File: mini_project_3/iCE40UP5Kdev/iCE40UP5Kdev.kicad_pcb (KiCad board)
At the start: 2 copper layers, 51 parts, among them J1 USB4105-GF-A, J2 Left, J3 Right, U1 W25Q32JV, U2 MIC5365-1-2YD5, U3 MIC5318-3-3YD5, U4 ICE40UP5K-SG48ITR, X1 IQXO-791

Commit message: Add start to layout of mini project 3
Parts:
- J1: footprint Connector_USB:USB_C_Receptacle_GCT_USB4105-xx-A_16P_TopMnt_Horizontal -> Eclectronics:USB4105-GF-A
- moved C2 110.6 mm to (154.7, 97.2), turned to 180 degrees
- moved C1 109.5 mm to (155.5, 91.5)
- moved C7 108.2 mm to (155.2, 104.7), turned to 90 degrees
- moved U4 107.4 mm to (150.3, 113.2), turned to 180 degrees
- moved R16 102.3 mm to (153.5, 107.4)
- moved C6 99.3 mm to (148.2, 96.6), turned to 90 degrees
- moved C4 98.3 mm to (146.5, 92.4), turned to 90 degrees
- moved C3 97.4 mm to (143.0, 93.4), turned to 90 degrees
- moved R4 96.6 mm to (152.0, 95.6), turned to -90 degrees
- moved C5 96.6 mm to (143.2, 96.7), turned to 90 degrees
- moved R15 96.0 mm to (150.3, 99.1), turned to 180 degrees
- moved R3 95.4 mm to (151.1, 92.3), turned to -90 degrees
- moved R2 94.4 mm to (148.1, 92.3), turned to -90 degrees
- moved R1 93.5 mm to (144.9, 92.4), turned to 90 degrees
- moved D2 91.0 mm to (150.1, 95.6), turned to -90 degrees
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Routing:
- net Net-(U1-DO/IO1): track 0.00 -> 19.3 mm
- net Net-(U1-~{CS}): track 0.00 -> 14.7 mm
- net Net-(U1-DI/IO0): track 0.00 -> 6.87 mm
- net Net-(U1-SCK): track 0.00 -> 4.19 mm
- net +3V3: track 0.00 -> 1.09 mm, vias 0 -> 1
- net GND: track 0.00 -> 0.97 mm, vias 0 -> 1
- net Net-(U3-EN): track 0.00 -> 0.66 mm

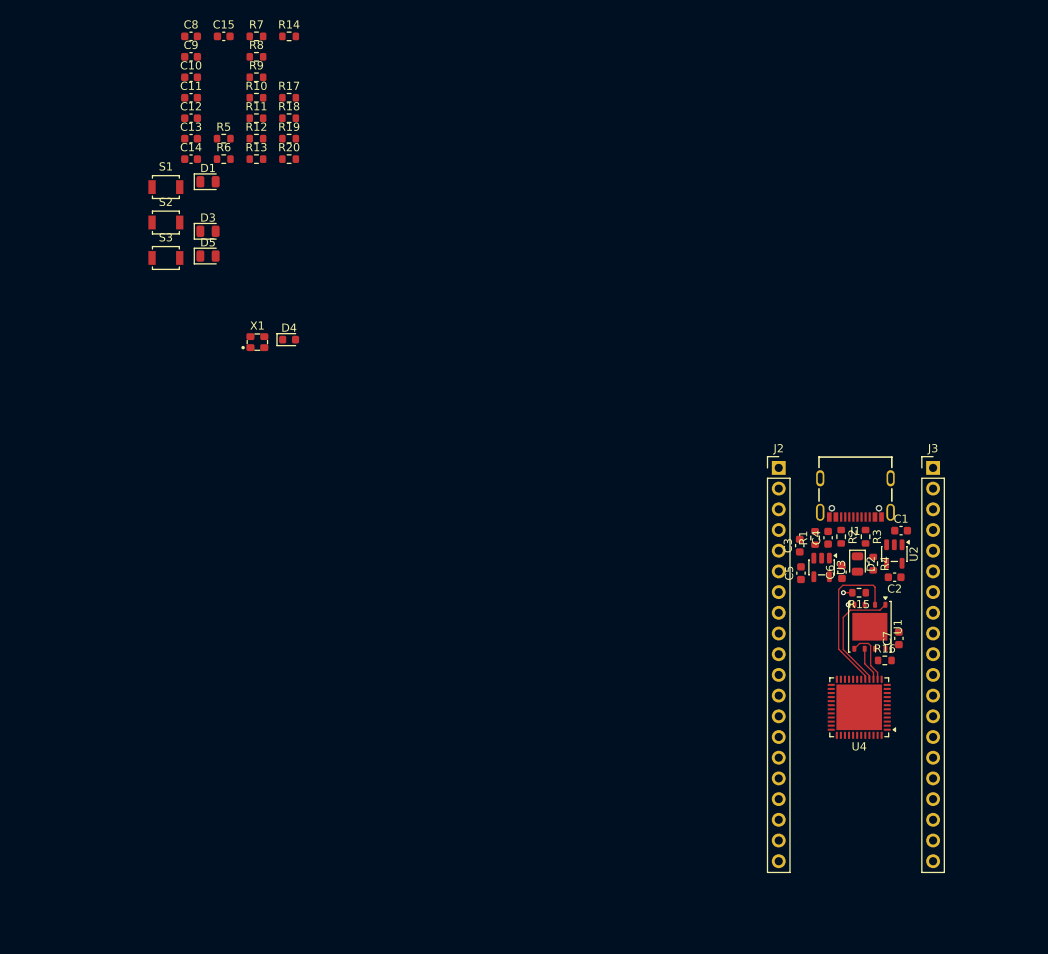
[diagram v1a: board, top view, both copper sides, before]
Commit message: Add more components to layout
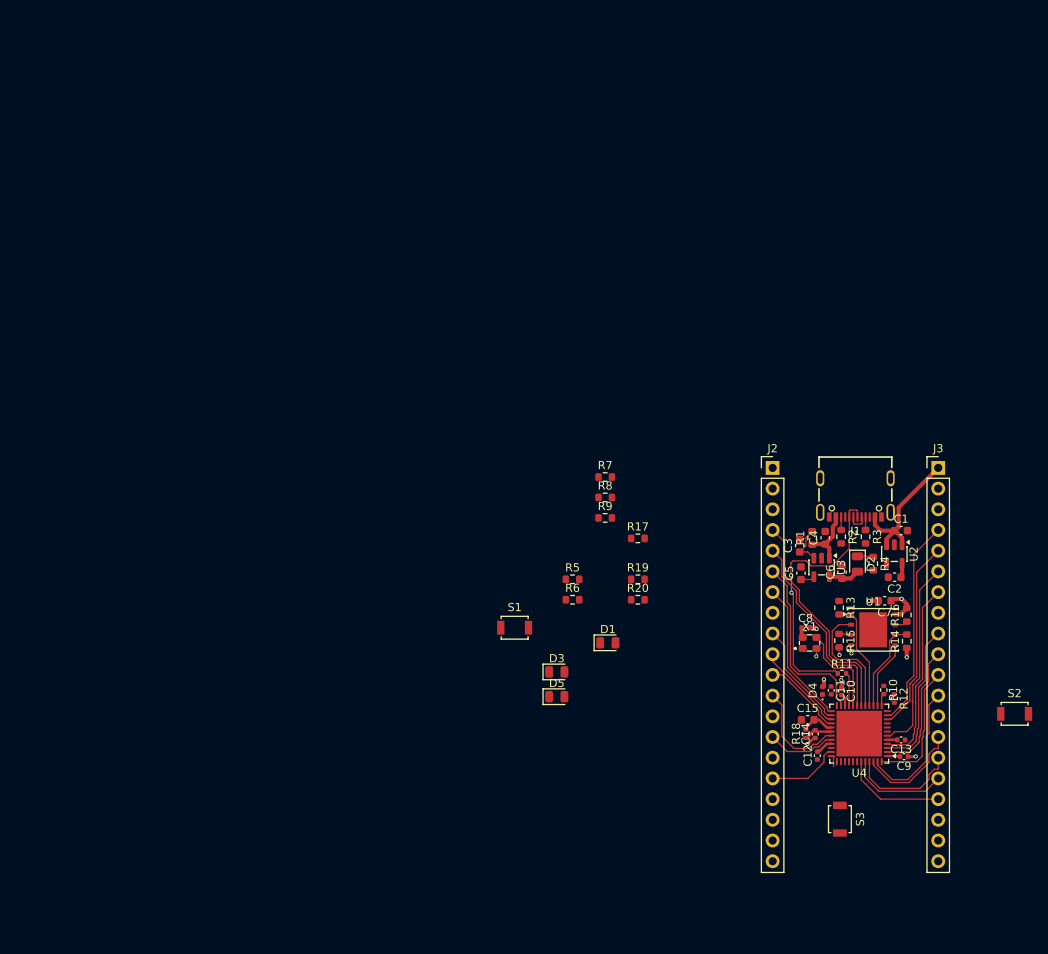
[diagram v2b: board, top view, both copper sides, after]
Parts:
- C10, C11, C12, C13, C14, C8, C9: footprint Capacitor_SMD:C_0603_1608Metric -> Capacitor_SMD:C_0402_1005Metric
- D4: footprint Diode_SMD:D_0603_1608Metric -> Diode_SMD:D_0402_1005Metric
- R10, R11, R12, R18: footprint Resistor_SMD:R_0603_1608Metric -> Resistor_SMD:R_0402_1005Metric
- moved C9 122.6 mm to (155.8, 119.3), turned to 180 degrees
- moved S2 120.3 mm to (169.4, 114.0)
- moved C13 114.2 mm to (155.5, 117.2), turned to 180 degrees
- moved C15 110.3 mm to (144.0, 114.7)
- moved C10 109.7 mm to (148.2, 111.2), turned to -90 degrees
- moved C12 109.6 mm to (145.2, 119.1), turned to 90 degrees
- moved S3 107.6 mm to (148.0, 126.9), turned to -90 degrees
- moved C11 107.0 mm to (146.9, 111.1), turned to -90 degrees
- moved R14 106.1 mm to (156.2, 105.1), turned to 90 degrees
- moved R10 105.9 mm to (153.3, 111.1), turned to -90 degrees
- moved C8 104.6 mm to (143.7, 103.4)
- moved R12 104.1 mm to (154.6, 112.1), turned to -90 degrees
- moved C14 104.1 mm to (144.9, 116.5), turned to 90 degrees
- moved R11 99.0 mm to (148.2, 109.0)
- moved R18 98.6 mm to (143.8, 116.4), turned to 90 degrees
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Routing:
- net Net-(J1-D+-PadA6): track 0.00 -> 33.4 mm, vias 0 -> 2
- net /IOB_31b: track 0.00 -> 27.5 mm
- net /IOB_20a: track 0.00 -> 25.6 mm
- net +5V: track 0.32 -> 25.7 mm
- net /IOB_29b: track 0.00 -> 24.7 mm
- net /IOB_13b: track 0.00 -> 23.8 mm
- net /IOB_18a: track 0.00 -> 23.6 mm
- net /IOB_8a: track 0.00 -> 22.8 mm
- net /IOT_37a: track 0.00 -> 22.2 mm
- net /IOB_9b: track 0.00 -> 18.2 mm
- net /IOT_36b: track 0.00 -> 17.8 mm
- net +3V3: track 1.09 -> 17.9 mm, vias 1 -> 4
- net /IOB_2a: track 0.00 -> 16.7 mm
- net /IOB_6a: track 0.00 -> 16.2 mm
- net /IOB_4a: track 0.00 -> 16.0 mm
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
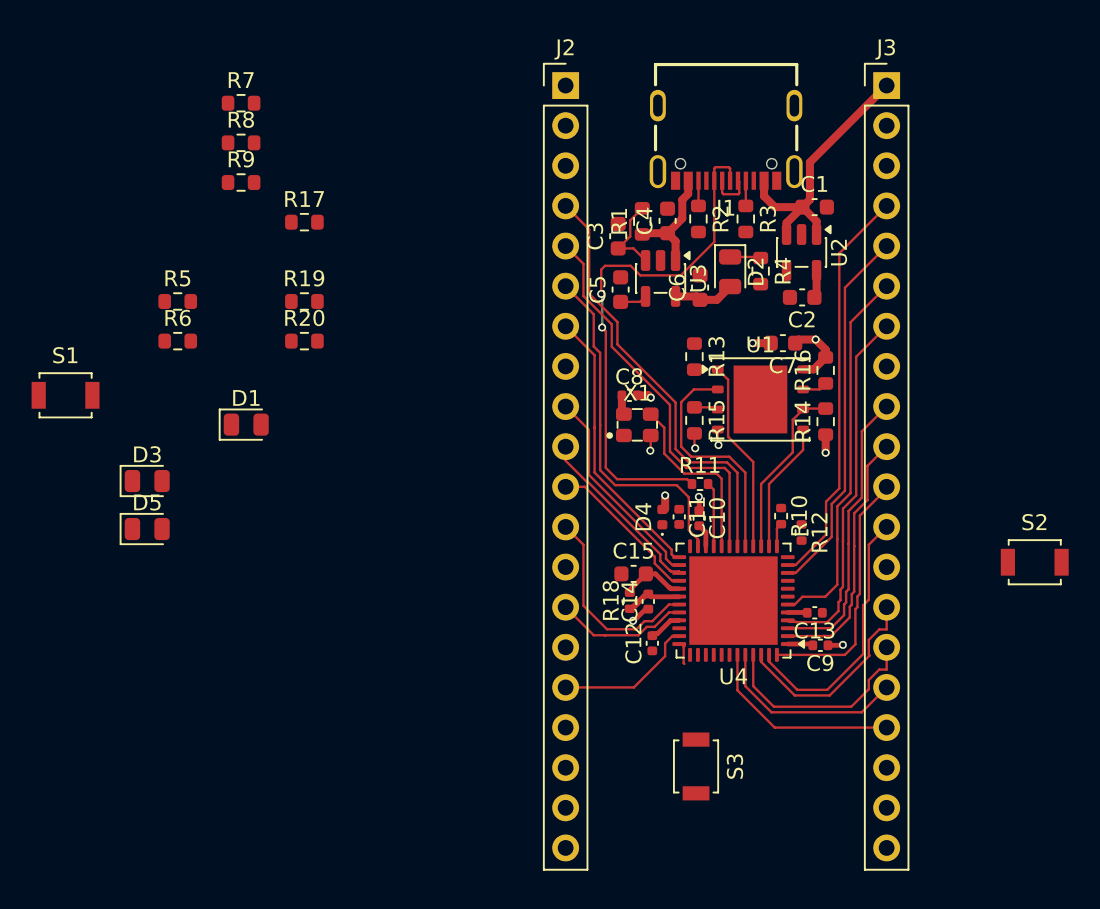
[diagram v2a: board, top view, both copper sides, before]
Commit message: Add more layout progress
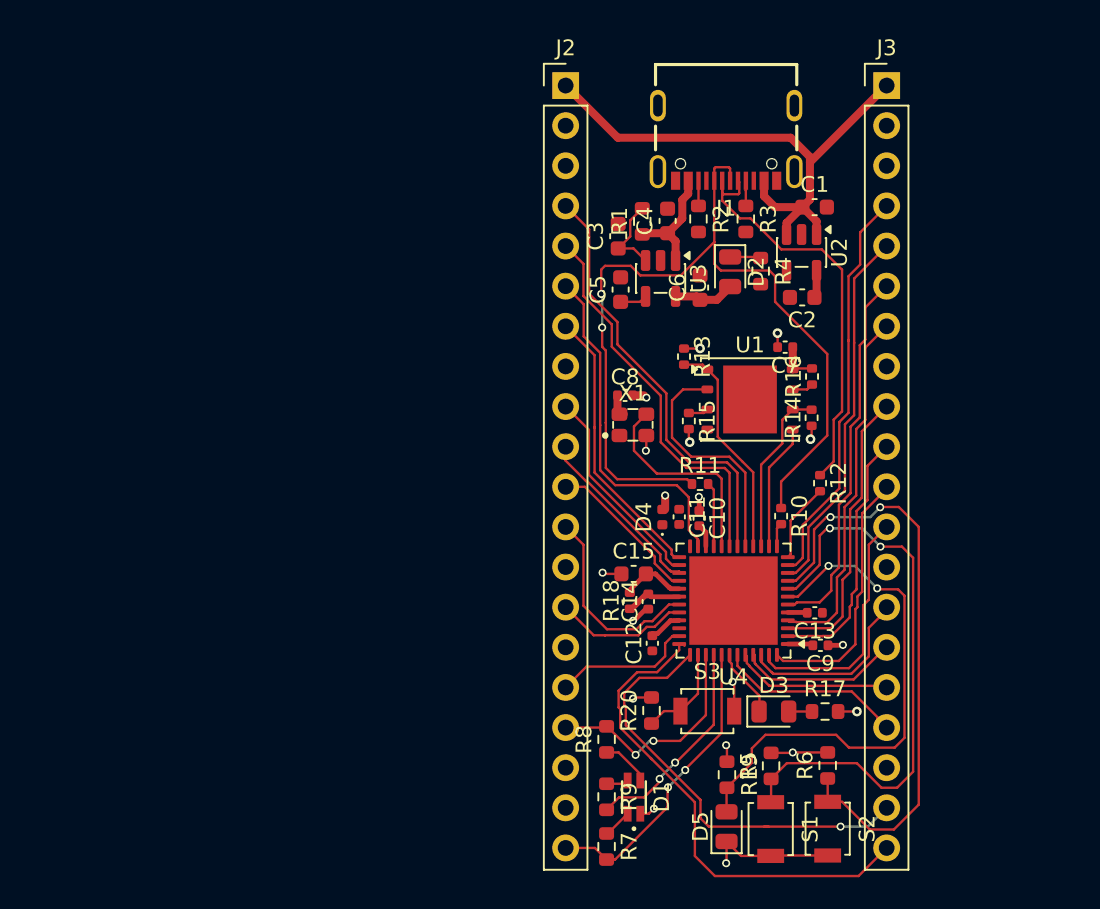
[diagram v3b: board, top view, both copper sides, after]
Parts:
- C7: footprint Capacitor_SMD:C_0603_1608Metric -> Capacitor_SMD:C_0402_1005Metric
- D1: footprint LED_SMD:LED_0805_2012Metric -> Eclectronics:IN-S85TATRGB
- R13, R14, R15, R16: footprint Resistor_SMD:R_0603_1608Metric -> Resistor_SMD:R_0402_1005Metric
- moved R7 52.4 mm to (142.3, 132.0), turned to -90 degrees
- moved S1 52.4 mm to (152.7, 130.9), turned to -90 degrees
- moved R6 49.1 mm to (156.3, 126.9), turned to 90 degrees
- moved R5 47.7 mm to (152.7, 126.9), turned to 90 degrees
- moved R9 45.2 mm to (142.3, 128.8), turned to -90 degrees
- moved R17 45.2 mm to (156.1, 123.4)
- moved R8 44.3 mm to (142.3, 125.2), turned to 90 degrees
- moved D3 42.3 mm to (152.9, 123.4)
- moved D5 41.2 mm to (149.9, 130.7), turned to 90 degrees
- moved R19 40.2 mm to (149.9, 127.4), turned to -90 degrees
- moved D1 34.0 mm to (144.0, 128.9), turned to 90 degrees
- moved R20 32.1 mm to (145.1, 123.4), turned to 90 degrees
- moved S2 21.4 mm to (156.3, 130.9), turned to -90 degrees
- moved S3 3.57 mm to (148.7, 123.4), turned to 0 degrees
- moved R12 3.34 mm to (155.8, 109.0)
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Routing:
- net Net-(U4-IOB_16a): track 0.00 -> 38.2 mm, vias 0 -> 2
- net Net-(U4-~{CRESET}): track 0.00 -> 37.0 mm, vias 0 -> 2
- net Net-(D5-A): track 0.00 -> 33.3 mm, vias 0 -> 2
- net /IOT_48b: track 1.92 -> 32.0 mm
- net /IOT_45a_G1: track 0.00 -> 27.9 mm, vias 0 -> 1
- net Net-(J1-D--PadA7): track 2.74 -> 27.0 mm
- net Net-(J1-D+-PadA6): track 33.4 -> 56.2 mm
- net /RGB2: track 0.00 -> 19.1 mm, vias 0 -> 2
- net +5V: track 25.7 -> 43.4 mm
- net /RGB0: track 0.00 -> 14.5 mm, vias 0 -> 2
- net /RGB1: track 0.00 -> 13.6 mm, vias 0 -> 2
- net GND: track 7.46 -> 17.3 mm, vias 7 -> 9
- net +3V3: track 17.9 -> 24.7 mm, vias 4 -> 9
- net /IOT_50b: track 0.00 -> 6.18 mm
- net Net-(U4-IOB_22a): track 0.00 -> 5.02 mm
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
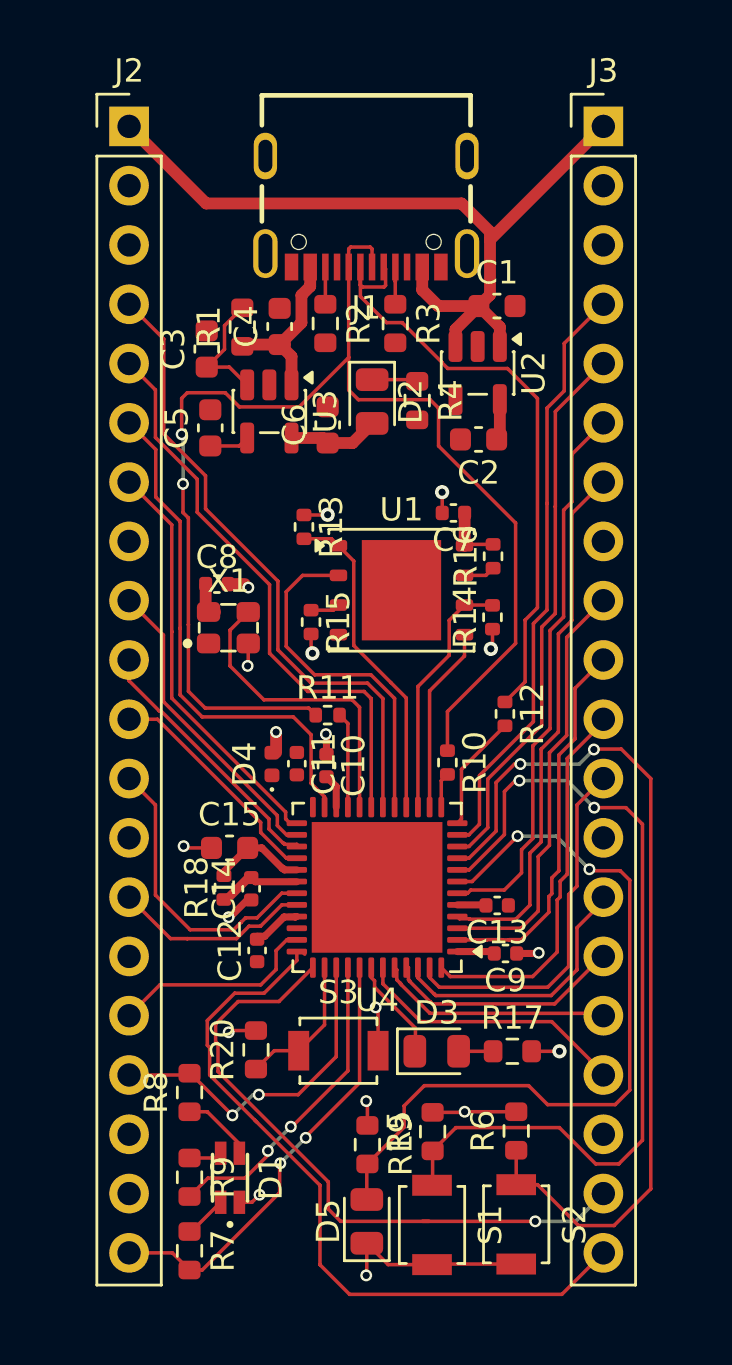
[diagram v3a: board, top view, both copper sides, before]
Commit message: Add layout with all components and most traces
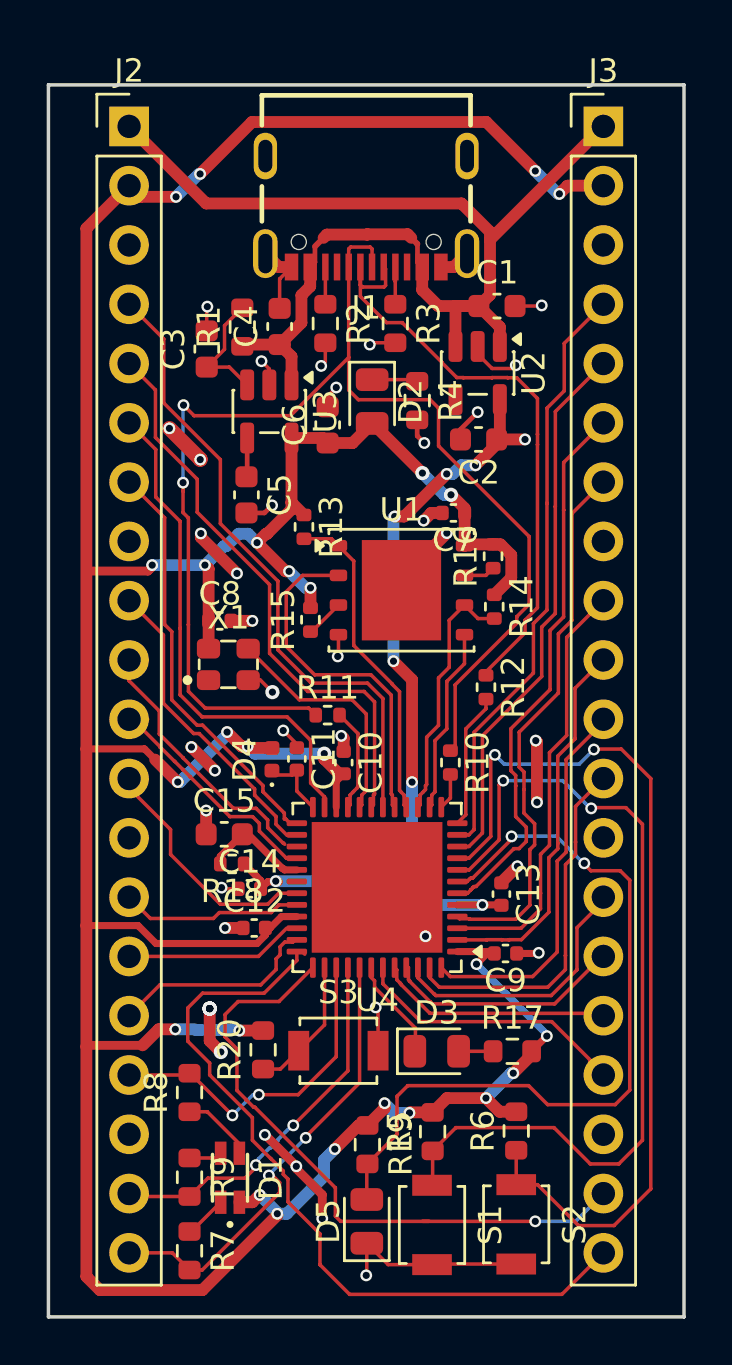
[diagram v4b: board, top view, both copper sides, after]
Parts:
- moved C5 3.26 mm to (144.7, 99.6), turned to -90 degrees
- moved C8 1.58 mm to (143.6, 105.0)
- moved X1 1.57 mm to (144.0, 106.9)
- moved R12 1.40 mm to (155.0, 107.8)
- moved R18 1.07 mm to (144.1, 115.4), turned to 180 degrees
- moved C12 0.97 mm to (145.1, 118.2), turned to 0 degrees
- moved C10 0.75 mm to (148.9, 111.1)
- moved C15 0.63 mm to (143.8, 114.1)
- moved C13 0.52 mm to (155.7, 116.7), turned to -90 degrees
- moved R14 0.46 mm to (155.3, 104.4), turned to -90 degrees
- moved R20 0.30 mm to (145.4, 123.4)
- moved C11 0.20 mm to (146.9, 110.9)
- moved D4 0.20 mm to (145.8, 110.9)
- moved R10 0.13 mm to (153.5, 111.1)
- moved R15 0.10 mm to (147.5, 105.0), turned to 90 degrees
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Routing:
- net +3V3: track 24.7 -> 178.3 mm, vias 9 -> 26
- net GND: track 17.3 -> 59.1 mm, vias 9 -> 41
- net +1V2: track 6.85 -> 39.3 mm, vias 0 -> 8
- net +5V: track 43.4 -> 50.8 mm
- net /IOT_44b: track 0.00 -> 7.25 mm
- net Net-(D4-K): track 0.00 -> 3.10 mm
- net Net-(U4-IOB_25b_G3): track 13.2 -> 10.3 mm
- net /RGB1: track 13.6 -> 16.2 mm
- net /IOT_42b: track 12.8 -> 10.5 mm
- net /IOT_48b: track 32.0 -> 33.4 mm
- net Net-(U4-IOB_16a): track 38.2 -> 39.2 mm
- net Net-(U4-IOB_22a): track 5.02 -> 5.82 mm
- net Net-(J1-D--PadA7): track 27.0 -> 26.2 mm
- net /IOT_43a: track 8.52 -> 7.81 mm
- net /IOB_8a: track 22.8 -> 23.4 mm
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- added copper zone on B.Cu, net GND
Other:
- board outline added: 27.2 x 52.8 mm

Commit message: Add nearly complete layout
Planning on trying to reduce the size of the board
by 100 mills after this commit to match the size
of a RasPi Pico
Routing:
- net GND: track 59.1 -> 70.3 mm, vias 41 -> 44
- net Net-(J1-D+-PadA6): track 56.5 -> 55.5 mm
